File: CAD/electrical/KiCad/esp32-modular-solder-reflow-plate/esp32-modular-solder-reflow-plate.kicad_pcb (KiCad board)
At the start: 2 copper layers, 81.3 x 50.8 mm, 100 parts, among them J1 Micro_SD, J2 USB-C, J3 I2C, J4 Thermo Coupler, J5 Heater, J6 PWR_IN, J7 Serial, J8 Buzzer, Q1 Heater N-FET, Q2 Q_PMOS_DGS, Q3 BUZ_CTL, SW1 µC_BTN01, SW2 µC_BTN02, SW3 µC_BTN03, SW4 µC_BTN04, SW5 µC_EN, SW6 µC_IO0, U1 MAX31855KASA, U2 ESP32-S3-WROOM-2, U3 AMS1117-3.3, U4 AMS1117-5.0, Y1 32k Hz

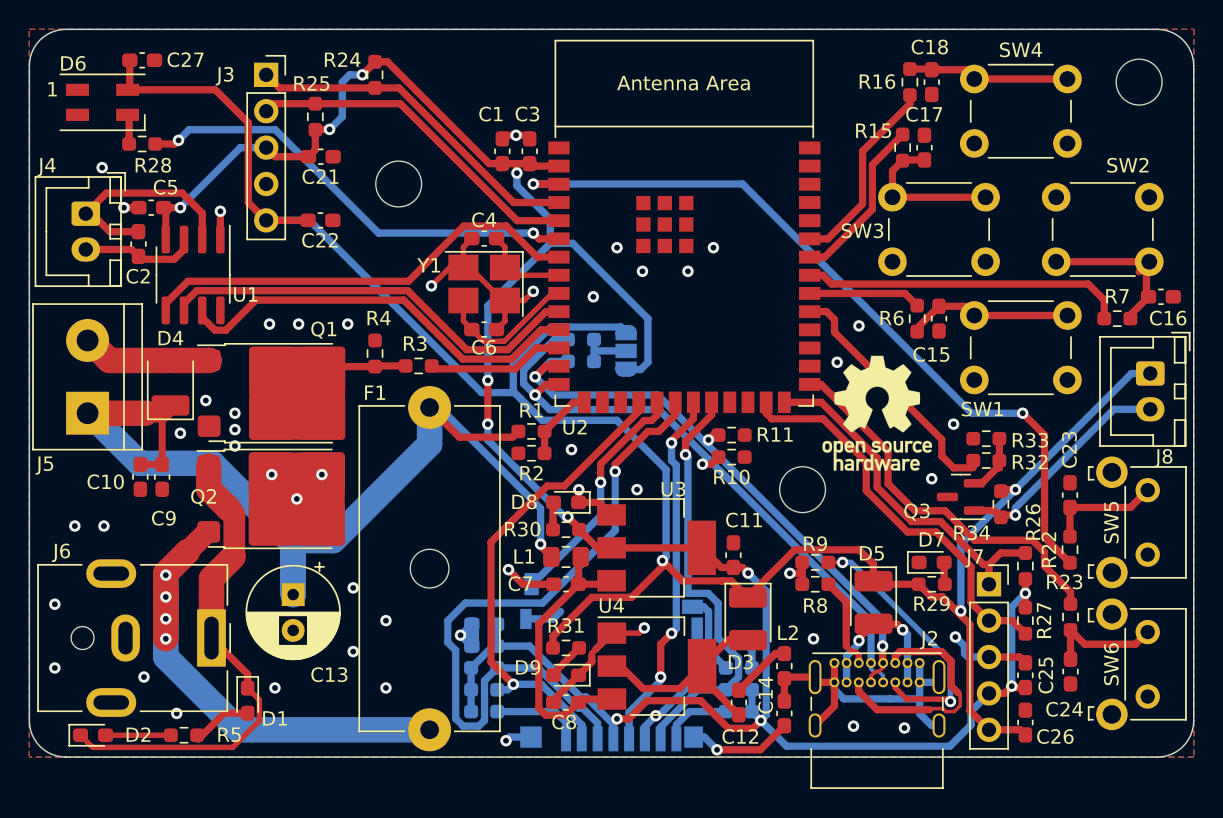
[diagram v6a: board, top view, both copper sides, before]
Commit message: - cad: minor routing improvements
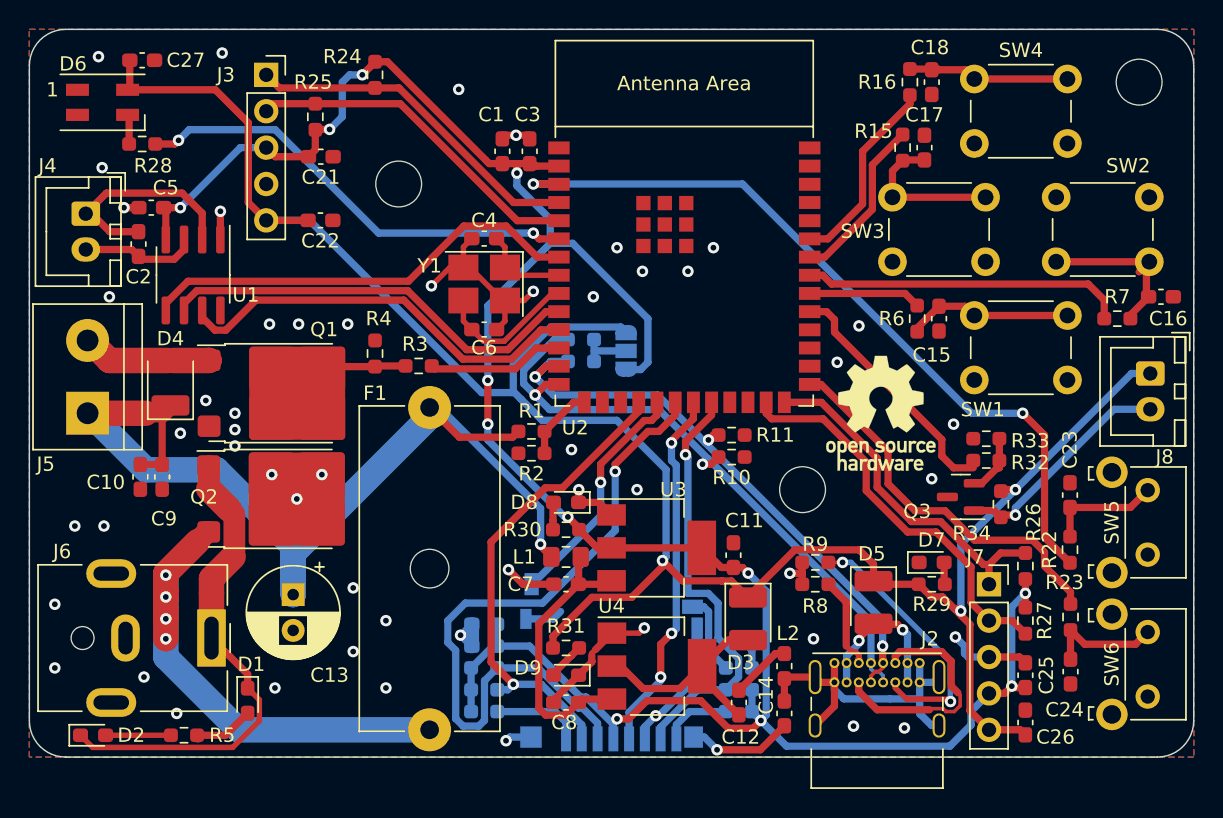
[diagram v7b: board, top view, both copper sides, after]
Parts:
- moved REF** 0.25 mm to (182.6, 83.3)
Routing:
- net HEATER_P: track 73.4 -> 71.8 mm
- net PWR_IN_N: vias 51 -> 55

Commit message: - cad: routing and silkscreen improvements
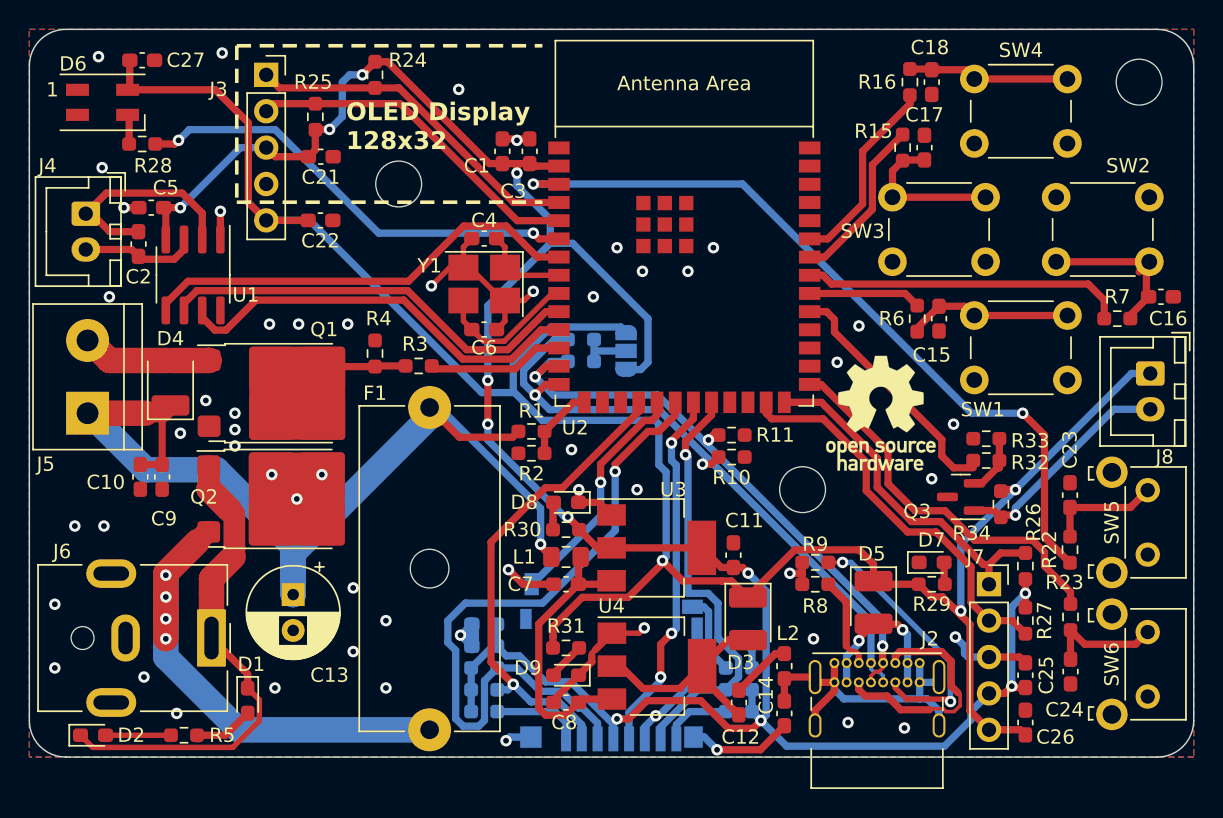
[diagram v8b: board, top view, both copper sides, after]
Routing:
- net PWR_IN_N: track 79.7 -> 77.2 mm
- net +5V: track 148.2 -> 150.1 mm
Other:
- board text added: "OLED Display 128x32"
